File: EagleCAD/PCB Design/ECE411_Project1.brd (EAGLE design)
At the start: 50 x 80 mm, 39 parts, among them U2 MIC29310-5.0WU, U3 NCP5501DT50RKG, U4 DCJACK_2.1MM_PTH

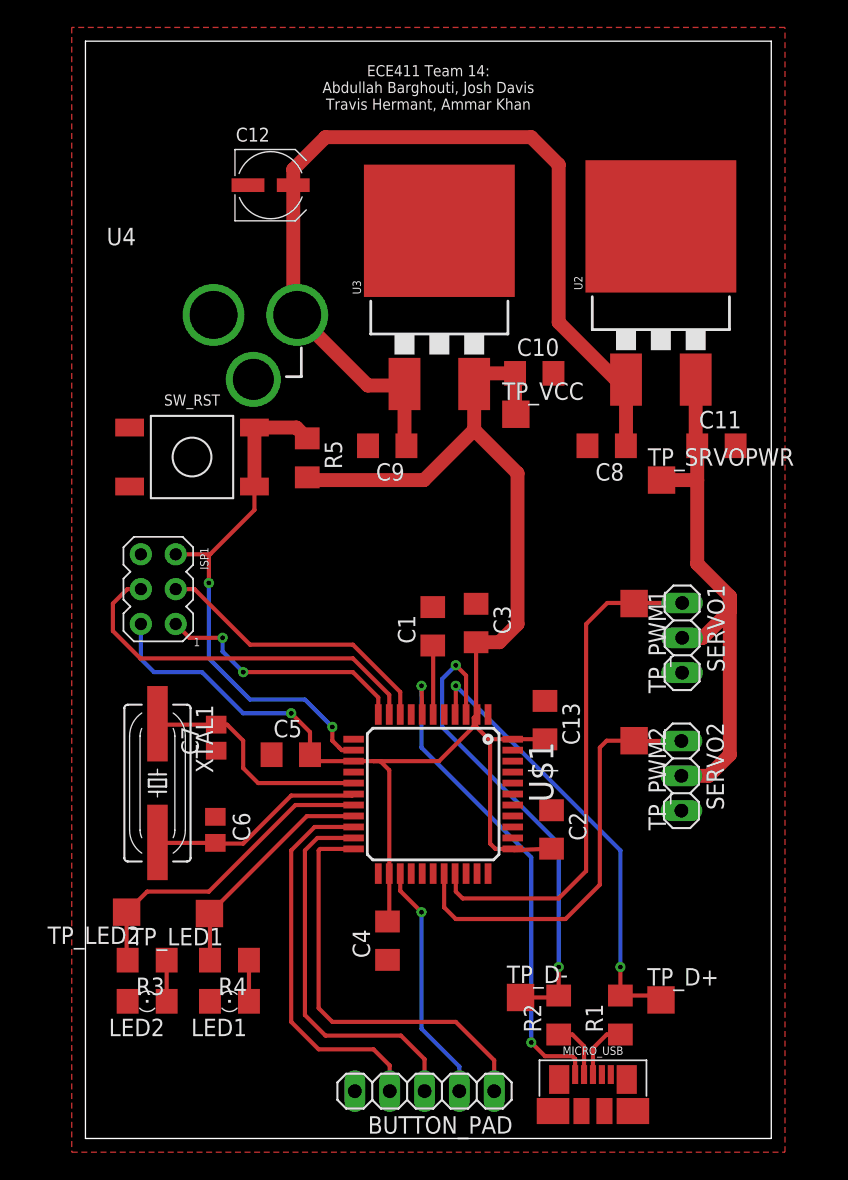
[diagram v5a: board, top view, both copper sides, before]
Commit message: Updated the Board Layout: Added stitching vias, double gnd planes, set isolate distance to 10mils, smashed all the components and made their tnames look cohesive.
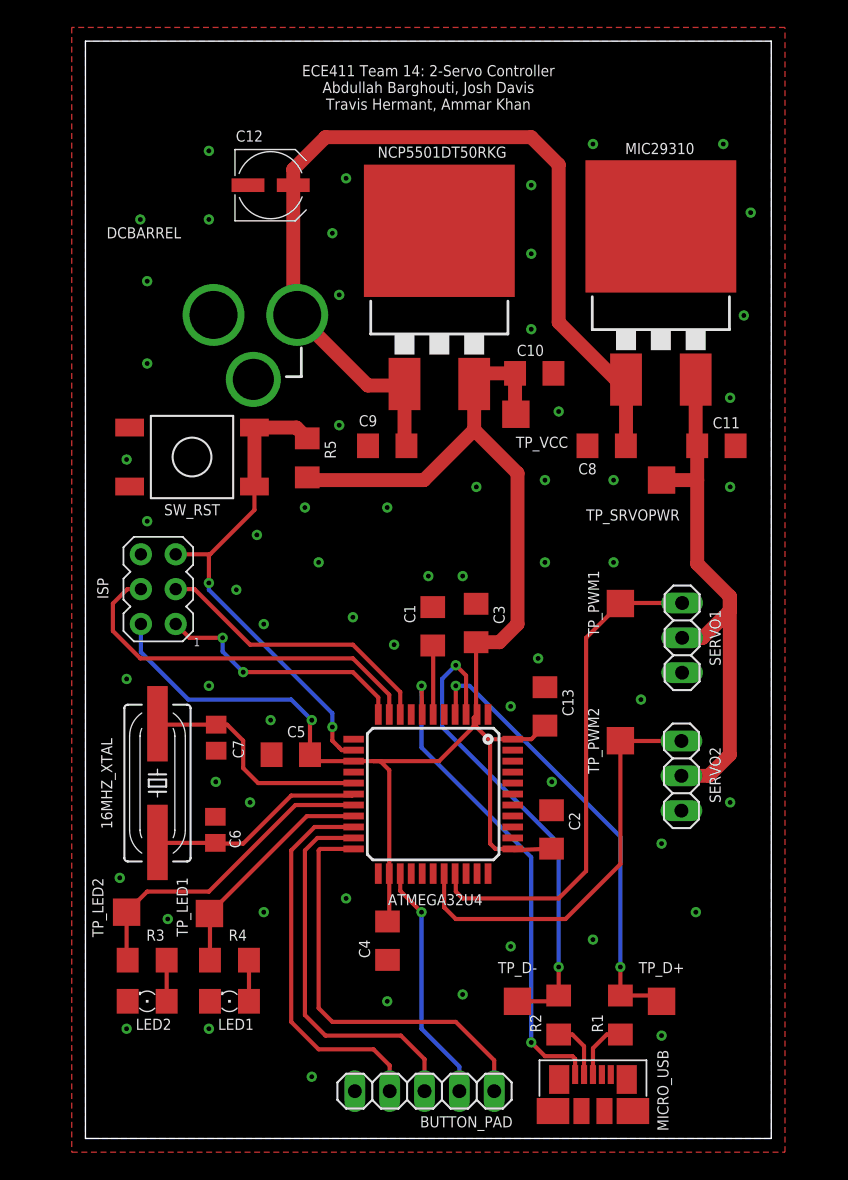
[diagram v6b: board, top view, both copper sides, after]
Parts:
- moved C13 1.00 mm to (33.5, 31.5)
- moved TP_PWM1 1.00 mm to (39.0, 39.0)
- moved TP_PWM2 1.00 mm to (39.0, 29.0)
- moved TP_D- 0.36 mm to (31.5, 10.0)
- moved TP_D+ 0.11 mm to (42.0, 10.0)
- renumbered ISP1 to ISP, U$1 to ATMEGA32U4, U2 to MIC29310, U3 to NCP5501DT50RKG, U4 to DCBARREL, XTAL1 to 16MHZ_XTAL
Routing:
- net /RST: track 38.8 -> 36.5 mm
- net VCC: track 111.8 -> 112.6 mm
- net PWM1: track 37.7 -> 37.0 mm
- net PWM2: track 31.4 -> 30.8 mm
- added copper zone on layer 16, net GND
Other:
- board text added: "ECE411 Team 14: 2-Servo Controller Abdullah Barghouti, Josh Davis Travis Hermant, Ammar Khan"
- board text removed: "ECE411 Team 14: Abdullah Barghouti, Josh Davis Travis Hermant, Ammar Khan"

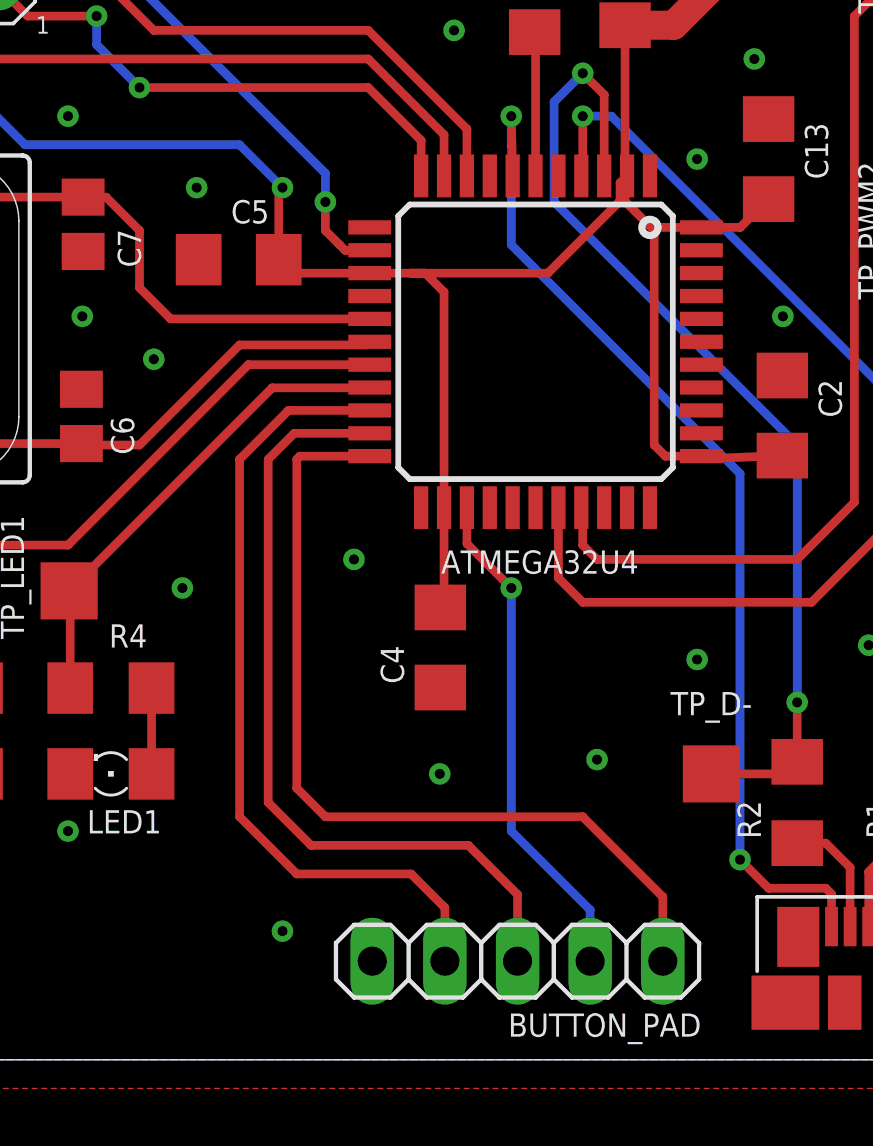
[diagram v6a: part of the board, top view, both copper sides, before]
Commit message: Updated board layout: moved power trace over so it wouldn't potentially bridge with the adjacent 32U4 pin; also moved button pad headers away from USB
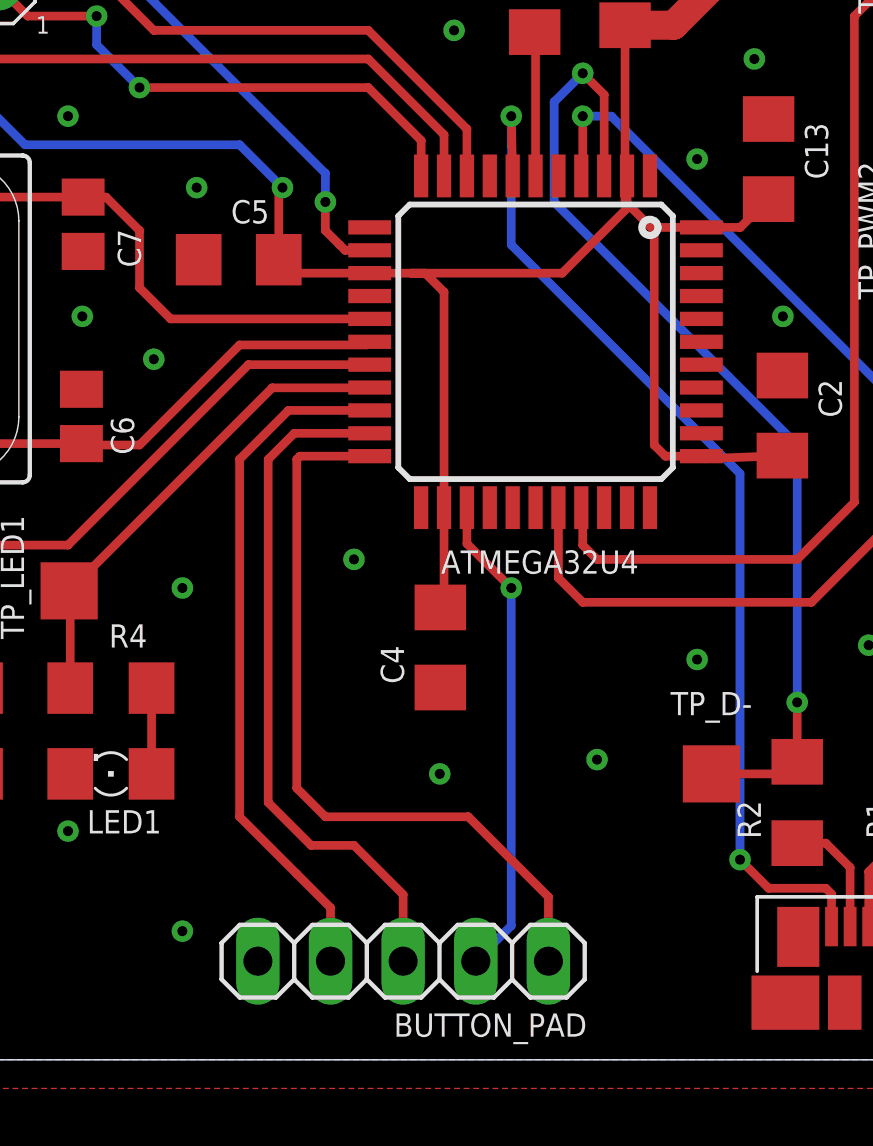
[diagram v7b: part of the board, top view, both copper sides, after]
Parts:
- moved BUTTON_PAD 4.00 mm to (20.7, 3.45)
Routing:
- net N$7: track 28.1 -> 24.1 mm
- net N$13: track 30.7 -> 26.7 mm
- net N$11: track 28.3 -> 24.3 mm
- net N$12: track 17.6 -> 17.0 mm
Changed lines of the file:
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@@
 <drawing>
 <settings>
-<setting alwaysvectorfont="yes"/>
+<setting alwaysvectorfont="no"/>
 <setting verticaltext="up"/>
 </settings>
@@
 </autorouter>
 <elements>
-<element name="BUTTON_PAD" library="pinhead" library_urn="urn:adsk.eagle:library:325" package="1X05" package3d_urn="urn:adsk.eagle:package:22469/2" value="" x="24.72" y="3.45" smashed="yes" rot="R180">
-<attribute name="NAME" x="31.1462" y="1.6212" size="0.8128" layer="25" font="vector" rot="R180"/>
-<attribute name="VALUE" x="31.07" y="6.625" size="1.27" layer="27" rot="R180"/>
+<element name="BUTTON_PAD" library="pinhead" library_urn="urn:adsk.eagle:library:325" package="1X05" package3d_urn="urn:adsk.eagle:package:22469/2" value="" x="20.72" y="3.45" smashed="yes" rot="R180">
+<attribute name="NAME" x="27.1462" y="1.6212" size="0.8128" layer="25" font="vector" rot="R180"/>
+<attribute name="VALUE" x="27.07" y="6.625" size="1.27" layer="27" rot="R180"/>
 </element>
 <element name="C1" library="rcl" library_urn="urn:adsk.eagle:library:334" package="C1206" package3d_urn="urn:adsk.eagle:package:23618/2" value="1u" x="25.32" y="37.34" smashed="yes" rot="R90">
@@
 <via x="6" y="16" extent="1-16" drill="0.35"/>
 <via x="13" y="16.5" extent="1-16" drill="0.35"/>
-<via x="16.5" y="4.5" extent="1-16" drill="0.35"/>
+<via x="13" y="4.5" extent="1-16" drill="0.35"/>
 <via x="42" y="21.5" extent="1-16" drill="0.35"/>
 <via x="40.5" y="32" extent="1-16" drill="0.35"/>
@@
 <wire x1="29.5" y1="29" x2="28.48" y2="30.02" width="0.3048" layer="1"/>
 <wire x1="28.48" y1="30.02" x2="28.48" y2="30.98" width="0.3048" layer="1"/>
-<wire x1="28.55" y1="30.91" x2="28.3048" y2="30.6648" width="0.3048" layer="1"/>
-<wire x1="28.3048" y1="30.6648" x2="28.3048" y2="30.03375" width="0.3048" layer="1"/>
-<wire x1="28.3048" y1="30.03375" x2="25.78105" y2="27.51" width="0.3048" layer="1"/>
-<wire x1="25.78105" y1="27.51" x2="21" y2="27.51" width="0.3048" layer="1"/>
+<wire x1="28.55" y1="29.77895" x2="26.28105" y2="27.51" width="0.3048" layer="1"/>
+<wire x1="26.28105" y1="27.51" x2="21" y2="27.51" width="0.3048" layer="1"/>
 <wire x1="28.34" y1="51.66" x2="24.68" y2="48" width="1.016" layer="1"/>
 <wire x1="16.368" y1="48" x2="16.17" y2="48.198" width="1.016" layer="1"/>
@@
 <wire x1="15" y1="32" x2="16.5" y2="30.5" width="0.3048" layer="16"/>
 <wire x1="4.04" y1="35.46" x2="7.5" y2="32" width="0.3048" layer="16"/>
+<wire x1="28.55" y1="30.91" x2="28.55" y2="29.77895" width="0.3048" layer="1"/>
 </signal>
 <signal name="PWM2">
@@
 <wire x1="15" y1="21" x2="15" y2="8.5" width="0.3048" layer="1"/>
 <wire x1="15" y1="8.5" x2="17" y2="6.5" width="0.3048" layer="1"/>
-<wire x1="22.18" y1="5.32" x2="22.18" y2="3.45" width="0.3048" layer="1"/>
+<wire x1="18.18" y1="5.32" x2="18.18" y2="3.45" width="0.3048" layer="1"/>
 <wire x1="16.71" y1="22.71" x2="15" y2="21" width="0.3048" layer="1"/>
-<wire x1="17" y1="6.5" x2="21" y2="6.5" width="0.3048" layer="1"/>
-<wire x1="21" y1="6.5" x2="22.18" y2="5.32" width="0.3048" layer="1"/>
+<wire x1="17" y1="6.5" x2="18.18" y2="5.32" width="0.3048" layer="1"/>
 </signal>
 <signal name="N$11">
@@
 <wire x1="16" y1="21" x2="16" y2="9" width="0.3048" layer="1"/>
 <wire x1="16" y1="9" x2="17.5" y2="7.5" width="0.3048" layer="1"/>
-<wire x1="24.72" y1="5.78" x2="24.72" y2="3.45" width="0.3048" layer="1"/>
+<wire x1="20.72" y1="5.78" x2="20.72" y2="3.45" width="0.3048" layer="1"/>
 <wire x1="16.91" y1="21.91" x2="16" y2="21" width="0.3048" layer="1"/>
-<wire x1="17.5" y1="7.5" x2="23" y2="7.5" width="0.3048" layer="1"/>
-<wire x1="23" y1="7.5" x2="24.72" y2="5.78" width="0.3048" layer="1"/>
+<wire x1="17.5" y1="7.5" x2="19" y2="7.5" width="0.3048" layer="1"/>
+<wire x1="19" y1="7.5" x2="20.72" y2="5.78" width="0.3048" layer="1"/>
 </signal>
 <signal name="N$12">
@@
 <via x="24.5" y="16.5" extent="1-16" drill="0.35"/>
 <wire x1="22.95" y1="18.05" x2="24.5" y2="16.5" width="0.3048" layer="1"/>
-<wire x1="24.5" y1="16.5" x2="24.5" y2="8" width="0.3048" layer="16"/>
-<wire x1="27.26" y1="5.24" x2="27.26" y2="3.45" width="0.3048" layer="16"/>
-<wire x1="24.5" y1="8" x2="27.26" y2="5.24" width="0.3048" layer="16"/>
+<wire x1="24.5" y1="16.5" x2="24.5" y2="4.69" width="0.3048" layer="16"/>
+<wire x1="24.5" y1="4.69" x2="23.26" y2="3.45" width="0.3048" layer="16"/>
 </signal>
 <signal name="N$13">
@@
 <wire x1="17" y1="21" x2="17" y2="9.5" width="0.3048" layer="1"/>
 <wire x1="17" y1="9.5" x2="18" y2="8.5" width="0.3048" layer="1"/>
-<wire x1="29.8" y1="5.7" x2="29.8" y2="3.45" width="0.3048" layer="1"/>
-<wire x1="18" y1="8.5" x2="27" y2="8.5" width="0.3048" layer="1"/>
-<wire x1="27" y1="8.5" x2="29.8" y2="5.7" width="0.3048" layer="1"/>
+<wire x1="25.8" y1="5.7" x2="25.8" y2="3.45" width="0.3048" layer="1"/>
+<wire x1="18" y1="8.5" x2="23" y2="8.5" width="0.3048" layer="1"/>
+<wire x1="23" y1="8.5" x2="25.8" y2="5.7" width="0.3048" layer="1"/>
 </signal>
 <signal name="N$17">

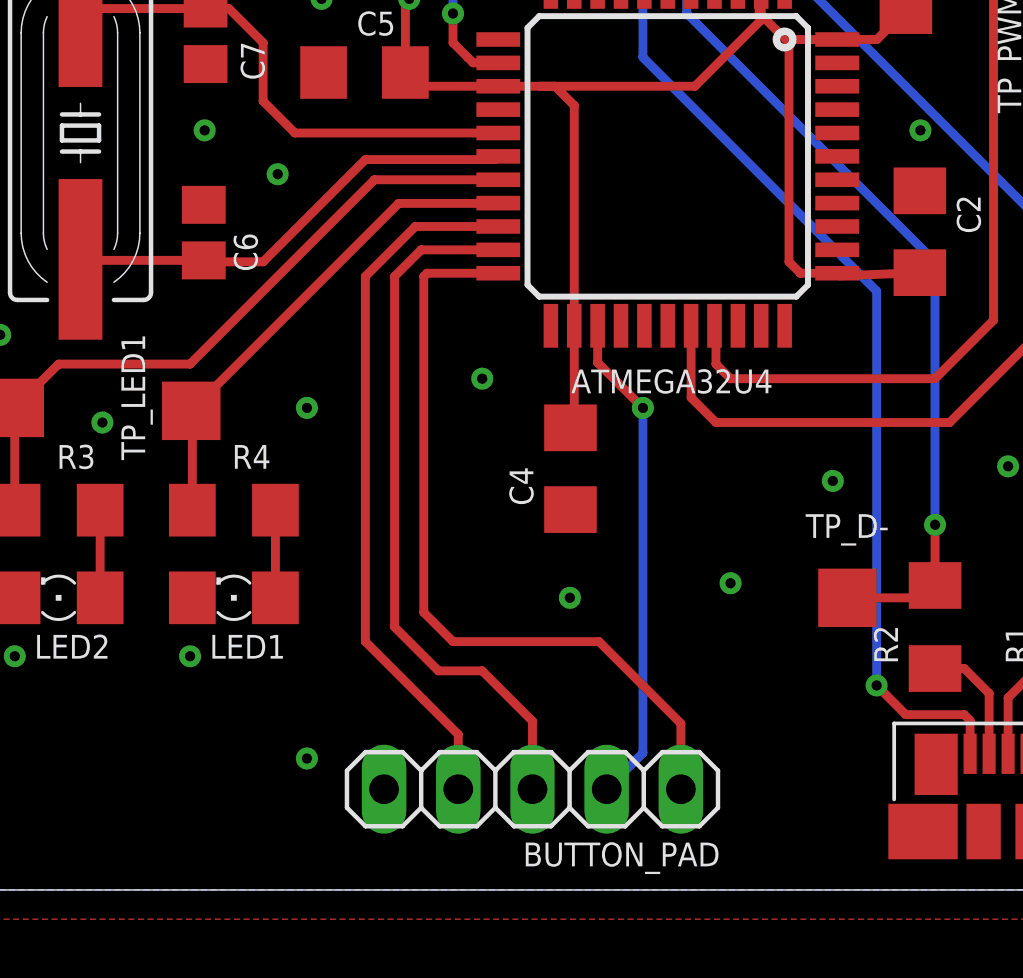
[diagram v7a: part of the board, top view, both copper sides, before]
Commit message: Changed the schematic: moved the LEDs, and outputted the whole D port to a 9-pin header, with the ninth pin going to ground for the button pad.
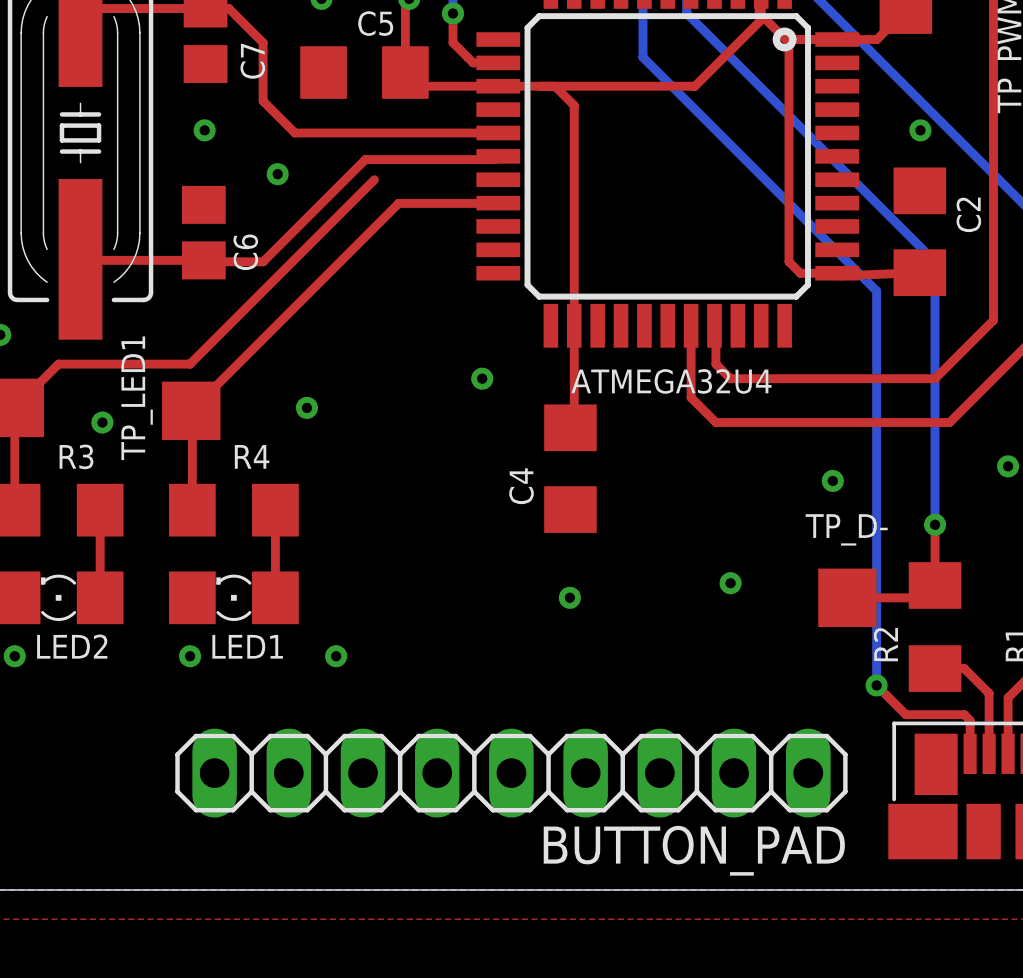
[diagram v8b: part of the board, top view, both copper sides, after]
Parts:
- BUTTON_PAD: device pinhead:1X05 -> pinhead:1X09
- moved BUTTON_PAD 0.91 mm to (20.0, 4.00)
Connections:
- removed net N$13: ATMEGA32U4.22, BUTTON_PAD.1
- new net N$1: ATMEGA32U4.27, BUTTON_PAD.1
- new net N$2: ATMEGA32U4.26, BUTTON_PAD.2
- new net N$3: ATMEGA32U4.22, BUTTON_PAD.3
- new net N$4: ATMEGA32U4.25, BUTTON_PAD.4
- new net N$5: ATMEGA32U4.21, BUTTON_PAD.5
- net GND: now also BUTTON_PAD.9; no longer BUTTON_PAD.5
- net N$11: now also ATMEGA32U4.19, BUTTON_PAD.7; no longer ATMEGA32U4.21, BUTTON_PAD.3
- net N$12: now also ATMEGA32U4.18, BUTTON_PAD.8; no longer ATMEGA32U4.25, BUTTON_PAD.2
- net N$6: now also ATMEGA32U4.32; no longer ATMEGA32U4.18
- net N$7: now also BUTTON_PAD.6; no longer BUTTON_PAD.4
- net N$8: now also ATMEGA32U4.31; no longer ATMEGA32U4.19
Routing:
- net N$13: track 26.7 -> 0.00 mm
- net N$11: track 24.3 -> 0.00 mm
- net N$7: track 24.1 -> 0.00 mm
- net N$12: track 17.0 -> 0.00 mm, vias 1 -> 0
- net N$6: track 23.3 -> 19.1 mm
